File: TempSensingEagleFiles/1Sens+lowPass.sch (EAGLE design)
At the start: 8 parts, among them U3 MLX90614_

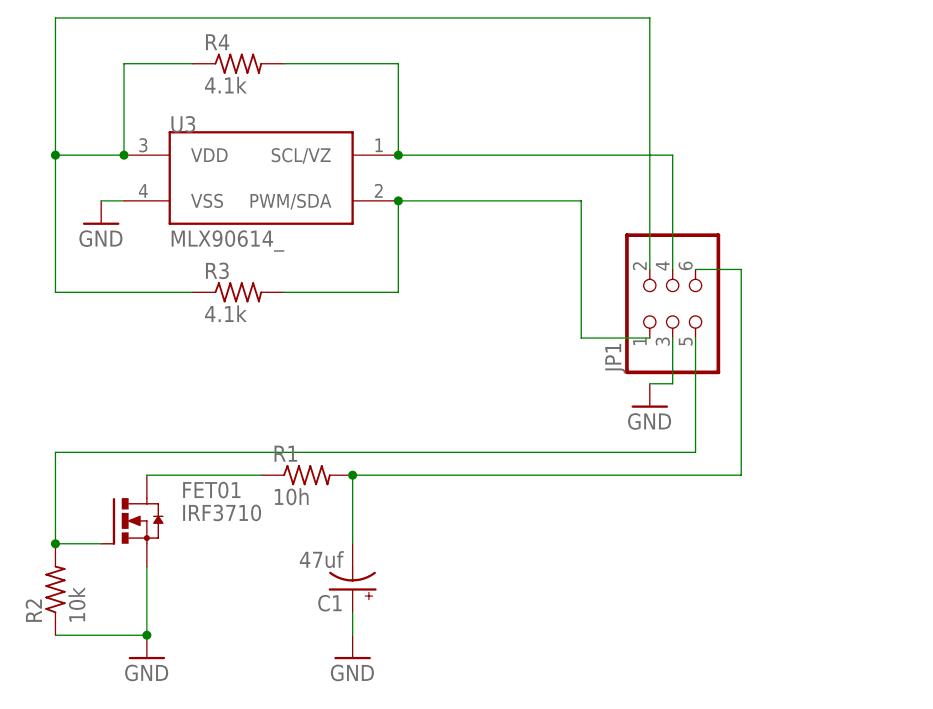
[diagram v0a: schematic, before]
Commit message: worked on Eagle Files
Added 1 Sensor and Main board
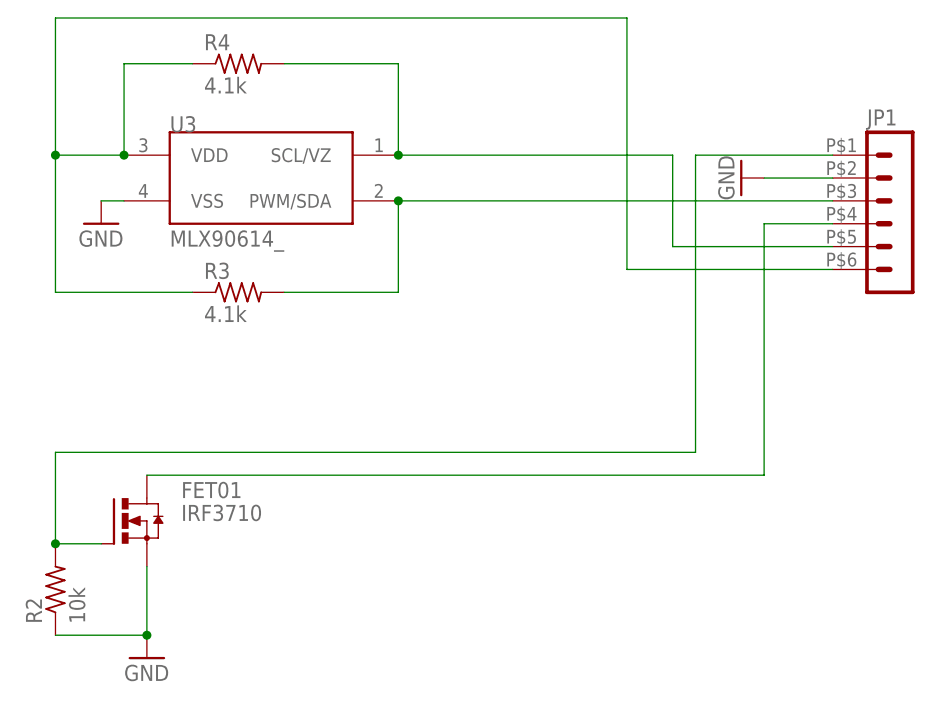
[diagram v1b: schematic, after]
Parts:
- removed C1: 47uf, rcl:CPOL-USE2,5-6E
- removed R1: 10h, rcl:R-US_0207/7
- JP1: device SparkFun-Connectors:PINHD-2X3 -> con-molex-micro-fit-3_0:HEADER_POS6_43045-0600
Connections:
- removed net N$11: C1.-, JP1.6, R1.2
- net GND: now also JP1.2; no longer C1.+, JP1.3
- net N$1: now also JP1.6; no longer JP1.2
- net N$15: now also JP1.5; no longer JP1.4
- net N$16: now also JP1.3; no longer JP1.1
- net N$18: now also JP1.1; no longer JP1.5
- net N$2: now also JP1.4; no longer R1.1
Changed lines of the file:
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@@
 <?xml version="1.0" encoding="utf-8"?>
 <!DOCTYPE eagle SYSTEM "eagle.dtd">
-<eagle version="6.4">
+<eagle version="6.6.0">
 <drawing>
 <settings>
@@
 <parts>
 <part name="FET01" library="transistor-power" deviceset="IRF3704" device="" value="IRF3710"/>
-<part name="C1" library="rcl" deviceset="CPOL-US" device="E2,5-6E" value="47uf"/>
-<part name="R1" library="rcl" deviceset="R-US_" device="0207/7" value="10h"/>
 <part name="R2" library="rcl" deviceset="R-US_" device="0207/7" value="10k"/>
 <part name="U3" library="SparkFun-Sensors" deviceset="MLX90614" device="_"/>
 <part name="R4" library="rcl" deviceset="R-US_" device="0204/5" value="4.1k"/>
 <part name="R3" library="rcl" deviceset="R-US_" device="0204/5" value="4.1k"/>
-<part name="GND2" library="supply1" deviceset="GND" device=""/>
 <part name="GND3" library="supply1" deviceset="GND" device=""/>
 <part name="GND4" library="supply1" deviceset="GND" device=""/>
-<part name="JP1" library="SparkFun-Connectors" deviceset="PINHD-2X3" device=""/>
+<part name="JP1" library="con-molex-micro-fit-3_0" deviceset="HEADER_POS6_?" device="43045-0600"/>
 <part name="GND5" library="supply1" deviceset="GND" device=""/>
 </parts>
@@
 <instances>
 <instance part="FET01" gate="G$1" x="139.7" y="68.58"/>
-<instance part="C1" gate="G$1" x="165.1" y="60.96" rot="R180"/>
-<instance part="R1" gate="G$1" x="160.02" y="73.66"/>
 <instance part="R2" gate="G$1" x="132.08" y="60.96" rot="R90"/>
 <instance part="U3" gate="G$1" x="154.94" y="106.68"/>
 <instance part="R4" gate="G$1" x="152.4" y="119.38"/>
 <instance part="R3" gate="G$1" x="152.4" y="93.98"/>
-<instance part="GND2" gate="1" x="165.1" y="53.34"/>
 <instance part="GND3" gate="1" x="142.24" y="53.34"/>
 <instance part="GND4" gate="1" x="137.16" y="101.6"/>
-<instance part="JP1" gate="A" x="200.66" y="91.44" rot="R90"/>
-<instance part="GND5" gate="1" x="198.12" y="81.28"/>
+<instance part="JP1" gate="G$1" x="223.52" y="101.6"/>
+<instance part="GND5" gate="1" x="208.28" y="106.68" rot="R270"/>
 </instances>
 <busses>
@@
 <wire x1="170.18" y1="109.22" x2="200.66" y2="109.22" width="0.1524" layer="91"/>
 <junction x="170.18" y="109.22"/>
-<pinref part="JP1" gate="A" pin="4"/>
-<wire x1="200.66" y1="96.52" x2="200.66" y2="109.22" width="0.1524" layer="91"/>
+<pinref part="JP1" gate="G$1" pin="5"/>
+<wire x1="200.66" y1="109.22" x2="200.66" y2="99.06" width="0.1524" layer="91"/>
+<wire x1="200.66" y1="99.06" x2="218.44" y2="99.06" width="0.1524" layer="91"/>
 </segment>
 </net>
@@
 <wire x1="170.18" y1="104.14" x2="170.18" y2="93.98" width="0.1524" layer="91"/>
 <wire x1="170.18" y1="93.98" x2="157.48" y2="93.98" width="0.1524" layer="91"/>
-<wire x1="170.18" y1="104.14" x2="190.5" y2="104.14" width="0.1524" layer="91"/>
-<wire x1="190.5" y1="104.14" x2="190.5" y2="88.9" width="0.1524" layer="91"/>
-<pinref part="JP1" gate="A" pin="1"/>
-<wire x1="190.5" y1="88.9" x2="198.12" y2="88.9" width="0.1524" layer="91"/>
 <junction x="170.18" y="104.14"/>
-</segment>
-</net>
-<net name="N$11" class="0">
-<segment>
-<pinref part="C1" gate="G$1" pin="-"/>
-<pinref part="R1" gate="G$1" pin="2"/>
-<wire x1="165.1" y1="66.04" x2="165.1" y2="73.66" width="0.1524" layer="91"/>
-<wire x1="165.1" y1="73.66" x2="208.28" y2="73.66" width="0.1524" layer="91"/>
-<junction x="165.1" y="73.66"/>
-<wire x1="208.28" y1="73.66" x2="208.28" y2="96.52" width="0.1524" layer="91"/>
-<pinref part="JP1" gate="A" pin="6"/>
-<wire x1="208.28" y1="96.52" x2="203.2" y2="96.52" width="0.1524" layer="91"/>
+<pinref part="JP1" gate="G$1" pin="3"/>
+<wire x1="170.18" y1="104.14" x2="218.44" y2="104.14" width="0.1524" layer="91"/>
 </segment>
 </net>
 <net name="N$18" class="0">
 <segment>
-<pinref part="JP1" gate="A" pin="5"/>
-<wire x1="203.2" y1="88.9" x2="203.2" y2="76.2" width="0.1524" layer="91"/>
 <pinref part="FET01" gate="G$1" pin="G"/>
 <pinref part="R2" gate="G$1" pin="2"/>
@@
 <wire x1="132.08" y1="76.2" x2="132.08" y2="66.04" width="0.1524" layer="91"/>
 <junction x="132.08" y="66.04"/>
+<pinref part="JP1" gate="G$1" pin="1"/>
+<wire x1="203.2" y1="76.2" x2="203.2" y2="109.22" width="0.1524" layer="91"/>
+<wire x1="203.2" y1="109.22" x2="218.44" y2="109.22" width="0.1524" layer="91"/>
 </segment>
 </net>
@@
 <wire x1="132.08" y1="109.22" x2="132.08" y2="124.46" width="0.1524" layer="91"/>
 <junction x="132.08" y="109.22"/>
-<wire x1="132.08" y1="124.46" x2="198.12" y2="124.46" width="0.1524" layer="91"/>
-<pinref part="JP1" gate="A" pin="2"/>
-<wire x1="198.12" y1="96.52" x2="198.12" y2="124.46" width="0.1524" layer="91"/>
+<wire x1="132.08" y1="124.46" x2="195.58" y2="124.46" width="0.1524" layer="91"/>
+<pinref part="JP1" gate="G$1" pin="6"/>
+<wire x1="195.58" y1="124.46" x2="195.58" y2="96.52" width="0.1524" layer="91"/>
+<wire x1="195.58" y1="96.52" x2="218.44" y2="96.52" width="0.1524" layer="91"/>
 </segment>
 </net>
 <net name="GND" class="0">
-<segment>
-<pinref part="C1" gate="G$1" pin="+"/>
-<wire x1="165.1" y1="55.88" x2="165.1" y2="58.42" width="0.1524" layer="91"/>
-<pinref part="GND2" gate="1" pin="GND"/>
-</segment>
 <segment>
 <pinref part="R2" gate="G$1" pin="1"/>
@@
 </segment>
 <segment>
-<pinref part="JP1" gate="A" pin="3"/>
 <pinref part="GND5" gate="1" pin="GND"/>
-<wire x1="200.66" y1="88.9" x2="200.66" y2="83.82" width="0.1524" layer="91"/>
-<wire x1="200.66" y1="83.82" x2="198.12" y2="83.82" width="0.1524" layer="91"/>
+<pinref part="JP1" gate="G$1" pin="2"/>
+<wire x1="210.82" y1="106.68" x2="218.44" y2="106.68" width="0.1524" layer="91"/>
 </segment>
 </net>
@@
 <segment>
 <pinref part="FET01" gate="G$1" pin="D"/>
-<pinref part="R1" gate="G$1" pin="1"/>
-<wire x1="154.94" y1="73.66" x2="142.24" y2="73.66" width="0.1524" layer="91"/>
-</segment>
-</net>
+<wire x1="142.24" y1="73.66" x2="210.82" y2="73.66" width="0.1524" layer="91"/>
+<wire x1="210.82" y1="73.66" x2="210.82" y2="101.6" width="0.1524" layer="91"/>
+<pinref part="JP1" gate="G$1" pin="4"/>
+<wire x1="210.82" y1="101.6" x2="218.44" y2="101.6" width="0.1524" layer="91"/>
+</segment>
+</net>
